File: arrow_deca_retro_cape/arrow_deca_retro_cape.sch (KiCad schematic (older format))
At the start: 23 parts, among them J1 PMOD_A, J2 P8_Male, J3 P9_Male, U1 AS4C32M16SB-7TIN, U2 AS4C32M16SB-7TIN, U3 74LVC1G04

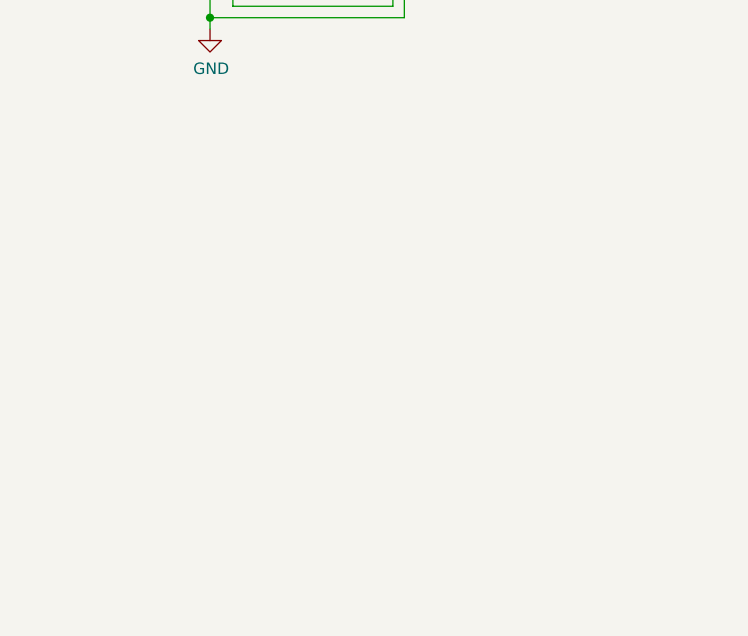
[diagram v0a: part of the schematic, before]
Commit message: Starting to add VGA.
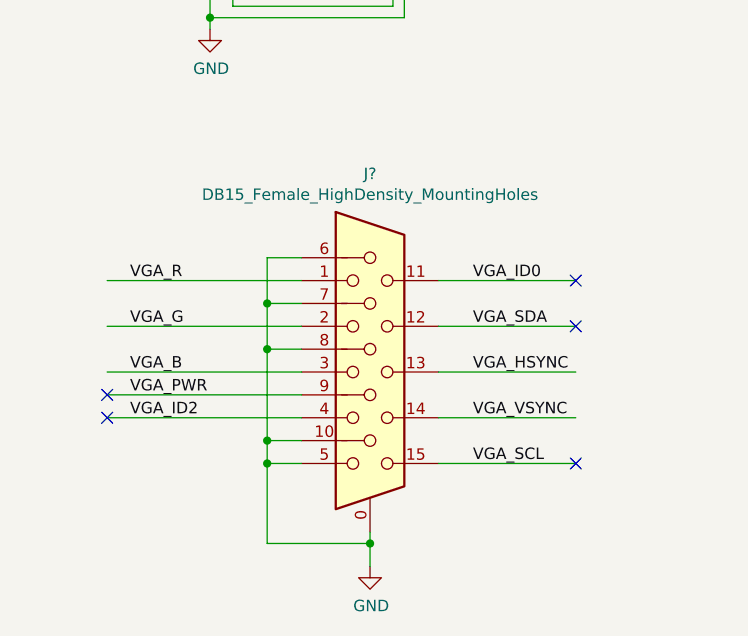
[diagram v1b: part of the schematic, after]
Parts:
- added J?: DB15_Female_HighDensity_MountingHoles, symbol Connector:DB15_Female_HighDensity_MountingHoles
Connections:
- net labels added: VGA_B, VGA_G, VGA_HSYNC, VGA_ID0, VGA_ID2, VGA_PWR, VGA_R, VGA_SCL, VGA_SDA, VGA_VSYNC
- wire segments 356 -> 379
- no-connect marks 0 -> 5
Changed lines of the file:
@@
 Wire Wire Line
 	14600 5700 14950 5700
+$Comp
+L Connector:DB15_Female_HighDensity_MountingHoles J?
+U 1 1 60D02E33
+P 2500 9700
+F 0 "J?" H 2500 10567 50  0000 C CNN
+F 1 "DB15_Female_HighDensity_MountingHoles" H 2500 10476 50  0000 C CNN
+F 2 "" H 1550 10100 50  0001 C CNN
+F 3 " ~" H 1550 10100 50  0001 C CNN
+	1    2500 9700
+	1    0    0    -1
+$EndComp
+$Comp
+L power:GND #PWR?
+U 1 1 60D07E5D
+P 2500 10550
+F 0 "#PWR?" H 2500 10300 50  0001 C CNN
+F 1 "GND" H 2505 10377 50  0000 C CNN
+F 2 "" H 2500 10550 50  0001 C CNN
+F 3 "" H 2500 10550 50  0001 C CNN
+	1    2500 10550
+	1    0    0    -1
+$EndComp
+Wire Wire Line
+	2500 10400 2500 10450
+Wire Wire Line
+	2800 9700 3400 9700
+Wire Wire Line
+	2800 9300 3400 9300
+Wire Wire Line
+	2800 9500 3400 9500
+Wire Wire Line
+	2800 9900 3400 9900
+Wire Wire Line
+	2800 10100 3400 10100
+Wire Wire Line
+	2200 10100 2050 10100
+Wire Wire Line
+	2050 10100 2050 10000
+Wire Wire Line
+	2050 9200 2200 9200
+Wire Wire Line
+	2050 10100 2050 10450
+Wire Wire Line
+	2050 10450 2500 10450
+Connection ~ 2050 10100
+Connection ~ 2500 10450
+Wire Wire Line
+	2500 10450 2500 10550
+Wire Wire Line
+	2200 9400 2050 9400
+Connection ~ 2050 9400
+Wire Wire Line
+	2050 9400 2050 9200
+Wire Wire Line
+	2200 9600 2050 9600
+Connection ~ 2050 9600
+Wire Wire Line
+	2050 9600 2050 9400
+Wire Wire Line
+	2200 10000 2050 10000
+Connection ~ 2050 10000
+Wire Wire Line
+	2050 9600 2050 10000
+Wire Wire Line
+	1350 9300 2200 9300
+Wire Wire Line
+	1350 9500 2200 9500
+Wire Wire Line
+	1350 9700 2200 9700
+Wire Wire Line
+	1350 9800 2200 9800
+NoConn ~ 3400 9300
+NoConn ~ 3400 9500
+Text Label 1450 9300 0    50   ~ 0
+VGA_R
+Text Label 1450 9500 0    50   ~ 0
+VGA_G
+Text Label 1450 9700 0    50   ~ 0
+VGA_B
+Text Label 1450 9800 0    50   ~ 0
+VGA_PWR
+NoConn ~ 1350 9800
+Wire Wire Line
+	1350 9900 2200 9900
+Text Label 1450 9900 0    50   ~ 0
+VGA_ID2
+NoConn ~ 1350 9900
+Text Label 2950 10100 0    50   ~ 0
+VGA_SCL
+Text Label 2950 9900 0    50   ~ 0
+VGA_VSYNC
+Text Label 2950 9700 0    50   ~ 0
+VGA_HSYNC
+Text Label 2950 9500 0    50   ~ 0
+VGA_SDA
+Text Label 2950 9300 0    50   ~ 0
+VGA_ID0
+NoConn ~ 3400 10100
 $EndSCHEMATC

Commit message: Layout finished.
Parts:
- removed J?: DB15_Female_HighDensity_MountingHoles, symbol Connector:DB15_Female_HighDensity_MountingHoles
- added J4: JOY0, snapeda:TE_1-1634580-2, symbol Connector:DB9_Male_MountingHoles
- added J5: MD-60SM, MD-60SM:MD-60SM, symbol MD60SM:MD-60SM
- added J6: JOY1, snapeda:TE_1-1634580-2, symbol Connector:DB9_Male_MountingHoles
- added R1, R2: 1K, Resistor_SMD:R_0603_1608Metric_Pad1.05x0.95mm_HandSolder, symbol Device:R
- added R10, R11, R12, R13, R14, R15, R16, R17, R18, R5, R6, R7, R8, R9: 2K, Resistor_SMD:R_0603_1608Metric_Pad1.05x0.95mm_HandSolder, symbol Device:R
- added R19, R20, R21, R22, R23, R24, R25, R26, R27, R28, R29, R30, R31, R32: 5K, Resistor_SMD:R_0603_1608Metric_Pad1.05x0.95mm_HandSolder, symbol Device:R
- added R3, R4: 10K, Resistor_SMD:R_0603_1608Metric_Pad1.05x0.95mm_HandSolder, symbol Device:R
- U1, U2: symbol AS4C32M16SB7TIN:AS4C32M16SB-7TIN -> arrow_deca_retro_cape-rescue:AS4C32M16SB-7TIN-AS4C32M16SB7TIN
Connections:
- net labels added: J0_DOWN, J0_LEFT, J0_PADDLE_A, J0_PADDLE_B, J0_RIGHT, J0_TRIGGER, J0_UP, J1_DOWN, J1_LEFT, J1_PADDLE_A, J1_PADDLE_B, J1_RIGHT, J1_TRIGGER, J1_UP, JOY0_DOWN, JOY0_LEFT, JOY0_PADDLE_A, JOY0_PADDLE_B, JOY0_RIGHT, JOY0_TRIGGER, JOY0_UP, JOY1_DOWN, JOY1_LEFT, JOY1_PADDLE_A, JOY1_PADDLE_B, JOY1_RIGHT, JOY1_TRIGGER, JOY1_UP, PS2_CLK, PS2_CLK_5V, PS2_DATA, PS2_DATA_5V
- net labels removed: GPIO1_D10, GPIO1_D11, GPIO1_D12, GPIO1_D13, GPIO1_D14, GPIO1_D15, GPIO1_D16, GPIO1_D17, GPIO1_D18, GPIO1_D19, GPIO1_D20, GPIO1_D21, GPIO1_D8, GPIO1_D9, VGA_B, VGA_G, VGA_HSYNC, VGA_ID0, VGA_ID2, VGA_PWR, VGA_R, VGA_SCL, VGA_SDA, VGA_VSYNC
- wire segments 379 -> 486
- no-connect marks 5 -> 16
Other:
- note added: "Mini-DIN 6P - PS2 Connector"
- moved on the sheet: J1

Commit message: rev1, sent to JLPCB.
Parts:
- added C18: 10uF, Capacitor_SMD:C_0805_2012Metric_Pad1.15x1.40mm_HandSolder, symbol Device:C
- added C19: 100uF, Capacitor_SMD:C_0805_2012Metric_Pad1.15x1.40mm_HandSolder, symbol Device:C
- added J7: Conn_01x03, Connector_PinHeader_2.54mm:PinHeader_1x03_P2.54mm_Vertical, symbol Connector_Generic:Conn_01x03
- added J8: Conn_01x06, Connector_PinHeader_2.54mm:PinHeader_1x06_P2.54mm_Vertical, symbol Connector_Generic:Conn_01x06
- added U4: LM1117-3.3, Package_TO_SOT_SMD:SOT-223-3_TabPin2, symbol Regulator_Linear:LM1117-3.3
- J1: value PMOD_A -> PMOD
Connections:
- net labels added: +3.3VP, 3V3_LDO, GPIO0, GPIO1, GPIO2, GPIO3, PMOD_D0, PMOD_D1, PMOD_D2, PMOD_D3, PMOD_D4, PMOD_D5, PMOD_D6, PMOD_D7
- net labels removed: GPIO1_D0, GPIO1_D1, GPIO1_D2, GPIO1_D22, GPIO1_D3, GPIO1_D4, GPIO1_D5, GPIO1_D6, GPIO1_D7
- wire segments 486 -> 510
- no-connect marks 16 -> 12
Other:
- note added: "Place jumper close to LDO"
